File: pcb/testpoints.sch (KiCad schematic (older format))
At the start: 0 parts

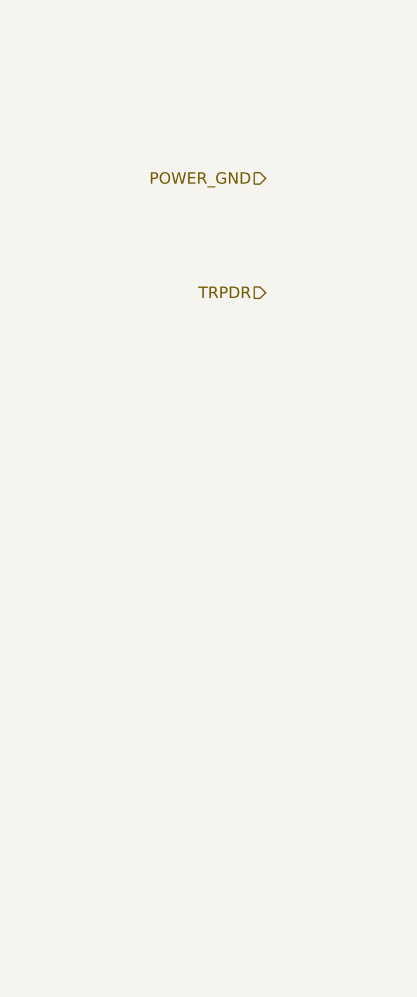
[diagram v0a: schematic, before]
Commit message: buffer section finished, audio moved to expansion connector
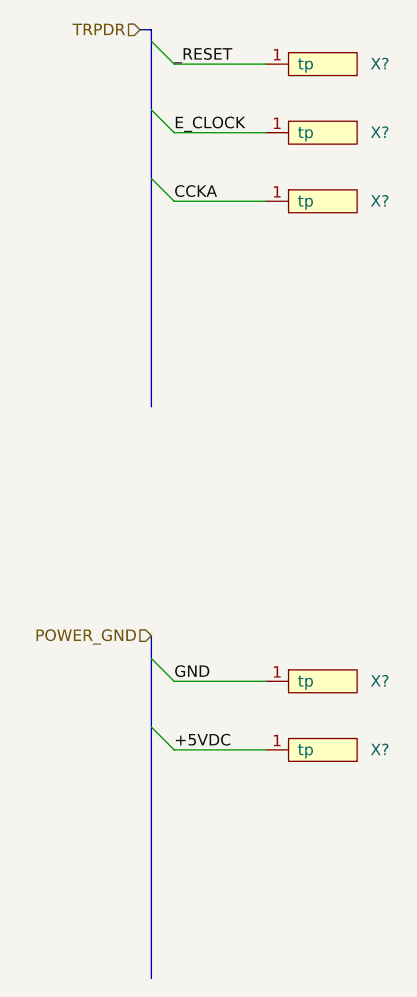
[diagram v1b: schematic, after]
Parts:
- added X? (x5): testpoint, symbol WM1200:testpoint
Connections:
- new net +5VDC: X?.1 (tp)
- new net CCKA: X?.1 (tp)
- new net E_CLOCK: X?.1 (tp)
- new net GND: X?.1 (tp)
- new net _RESET: X?.1 (tp)
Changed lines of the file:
@@
 Comment4 ""
 $EndDescr
-Text HLabel 1500 1500 0    50   Input ~ 0
+Text HLabel 1000 3500 0    50   Input ~ 0
 POWER_GND
-Text HLabel 1500 2000 0    50   Input ~ 0
+Text HLabel 950  850  0    50   Input ~ 0
 TRPDR
+$Comp
+L WM1200:testpoint X?
+U 1 1 5E702FA3
+P 1750 1050
+F 0 "X?" H 2000 1100 50  0000 C CNN
+F 1 "testpoint" H 1750 1200 50  0001 C CNN
+F 2 "" H 1750 1050 50  0001 C CNN
+F 3 "" H 1750 1050 50  0001 C CNN
+	1    1750 1050
+	1    0    0    -1
+$EndComp
+$Comp
+L WM1200:testpoint X?
+U 1 1 5E70432E
+P 1750 1350
+F 0 "X?" H 2000 1400 50  0000 C CNN
+F 1 "testpoint" H 1750 1500 50  0001 C CNN
+F 2 "" H 1750 1350 50  0001 C CNN
+F 3 "" H 1750 1350 50  0001 C CNN
+	1    1750 1350
+	1    0    0    -1
+$EndComp
+$Comp
+L WM1200:testpoint X?
+U 1 1 5E705858
+P 1750 1650
+F 0 "X?" H 2000 1700 50  0000 C CNN
+F 1 "testpoint" H 1750 1800 50  0001 C CNN
+F 2 "" H 1750 1650 50  0001 C CNN
+F 3 "" H 1750 1650 50  0001 C CNN
+	1    1750 1650
+	1    0    0    -1
+$EndComp
+Wire Bus Line
+	1000 850  950  850
+Entry Wire Line
+	1000 900  1100 1000
+Entry Wire Line
+	1000 1200 1100 1300
+Entry Wire Line
+	1000 1500 1100 1600
+Wire Wire Line
+	1100 1000 1500 1000
+Wire Wire Line
+	1500 1300 1100 1300
+Wire Wire Line
+	1100 1600 1500 1600
+Text Label 1100 1000 0    50   ~ 0
+_RESET
+Text Label 1100 1300 0    50   ~ 0
+E_CLOCK
+Text Label 1100 1600 0    50   ~ 0
+CCKA
+$Comp
+L WM1200:testpoint X?
+U 1 1 5E70BC9E
+P 1750 3750
+F 0 "X?" H 2000 3800 50  0000 C CNN
+F 1 "testpoint" H 1750 3900 50  0001 C CNN
+F 2 "" H 1750 3750 50  0001 C CNN
+F 3 "" H 1750 3750 50  0001 C CNN
+	1    1750 3750
+	1    0    0    -1
+$EndComp
+$Comp
+L WM1200:testpoint X?
+U 1 1 5E70BCA4
+P 1750 4050
+F 0 "X?" H 2000 4100 50  0000 C CNN
+F 1 "testpoint" H 1750 4200 50  0001 C CNN
+F 2 "" H 1750 4050 50  0001 C CNN
+F 3 "" H 1750 4050 50  0001 C CNN
+	1    1750 4050
+	1    0    0    -1
+$EndComp
+Entry Wire Line
+	1000 3600 1100 3700
+Entry Wire Line
+	1000 3900 1100 4000
+Wire Wire Line
+	1100 3700 1500 3700
+Wire Wire Line
+	1500 4000 1100 4000
+Text Label 1100 3700 0    50   ~ 0
+GND
+Text Label 1100 4000 0    50   ~ 0
++5VDC
+Wire Bus Line
+	1000 3500 1000 5000
+Wire Bus Line
+	1000 850  1000 2500
 $EndSCHEMATC

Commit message: Some work done on the whole project
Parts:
- gave numbers to parts that had none: 5
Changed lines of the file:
@@
 TRPDR
 $Comp
-L WM1200:testpoint X?
+L WM1200:testpoint XT1
 U 1 1 5E702FA3
 P 1750 1050
-F 0 "X?" H 2000 1100 50  0000 C CNN
+F 0 "XT1" H 2000 1100 50  0000 C CNN
 F 1 "testpoint" H 1750 1200 50  0001 C CNN
 F 2 "" H 1750 1050 50  0001 C CNN
@@
 $EndComp
 $Comp
-L WM1200:testpoint X?
+L WM1200:testpoint XT2
 U 1 1 5E70432E
 P 1750 1350
-F 0 "X?" H 2000 1400 50  0000 C CNN
+F 0 "XT2" H 2000 1400 50  0000 C CNN
 F 1 "testpoint" H 1750 1500 50  0001 C CNN
 F 2 "" H 1750 1350 50  0001 C CNN
@@
 $EndComp
 $Comp
-L WM1200:testpoint X?
+L WM1200:testpoint XT3
 U 1 1 5E705858
 P 1750 1650
-F 0 "X?" H 2000 1700 50  0000 C CNN
+F 0 "XT3" H 2000 1700 50  0000 C CNN
 F 1 "testpoint" H 1750 1800 50  0001 C CNN
 F 2 "" H 1750 1650 50  0001 C CNN
@@
 CCKA
 $Comp
-L WM1200:testpoint X?
+L WM1200:testpoint XT4
 U 1 1 5E70BC9E
 P 1750 3750
-F 0 "X?" H 2000 3800 50  0000 C CNN
+F 0 "XT4" H 2000 3800 50  0000 C CNN
 F 1 "testpoint" H 1750 3900 50  0001 C CNN
 F 2 "" H 1750 3750 50  0001 C CNN
@@
 $EndComp
 $Comp
-L WM1200:testpoint X?
+L WM1200:testpoint XT5
 U 1 1 5E70BCA4
 P 1750 4050
-F 0 "X?" H 2000 4100 50  0000 C CNN
+F 0 "XT5" H 2000 4100 50  0000 C CNN
 F 1 "testpoint" H 1750 4200 50  0001 C CNN
 F 2 "" H 1750 4050 50  0001 C CNN

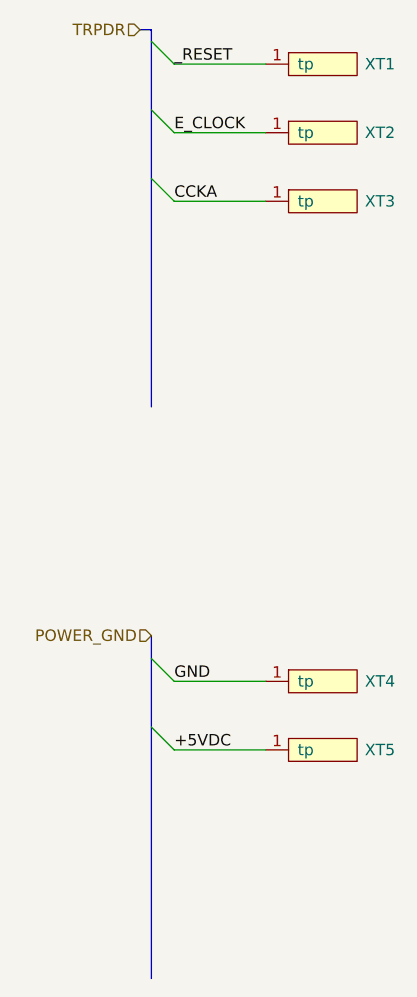
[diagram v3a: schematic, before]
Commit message: ok, we are using global labels now
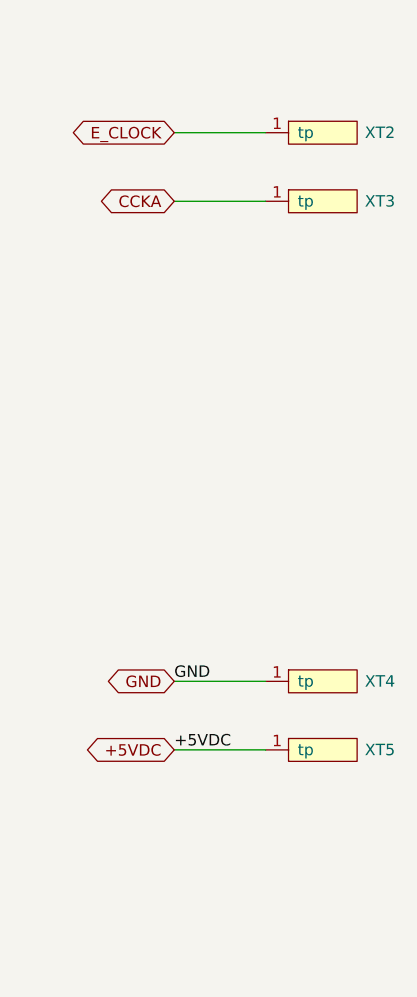
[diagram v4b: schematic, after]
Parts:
- removed XT1: testpoint, symbol WM1200:testpoint
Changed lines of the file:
@@
 $Descr A4 11693 8268
 encoding utf-8
-Sheet 4 11
+Sheet 2 11
 Title "WishMaster 1200"
 Date ""
@@
 Comment4 ""
 $EndDescr
-Text HLabel 1000 3500 0    50   Input ~ 0
-POWER_GND
-Text HLabel 950  850  0    50   Input ~ 0
-TRPDR
-$Comp
-L WM1200:testpoint XT1
-U 1 1 5E702FA3
-P 1750 1050
-F 0 "XT1" H 2000 1100 50  0000 C CNN
-F 1 "testpoint" H 1750 1200 50  0001 C CNN
-F 2 "" H 1750 1050 50  0001 C CNN
-F 3 "" H 1750 1050 50  0001 C CNN
-	1    1750 1050
-	1    0    0    -1
-$EndComp
 $Comp
 L WM1200:testpoint XT2
@@
 	1    0    0    -1
 $EndComp
-Wire Bus Line
-	1000 850  950  850
-Entry Wire Line
-	1000 900  1100 1000
-Entry Wire Line
-	1000 1200 1100 1300
-Entry Wire Line
-	1000 1500 1100 1600
-Wire Wire Line
-	1100 1000 1500 1000
 Wire Wire Line
 	1500 1300 1100 1300
 Wire Wire Line
 	1100 1600 1500 1600
-Text Label 1100 1000 0    50   ~ 0
-_RESET
-Text Label 1100 1300 0    50   ~ 0
-E_CLOCK
-Text Label 1100 1600 0    50   ~ 0
-CCKA
 $Comp
 L WM1200:testpoint XT4
@@
 	1    0    0    -1
 $EndComp
-Entry Wire Line
-	1000 3600 1100 3700
-Entry Wire Line
-	1000 3900 1100 4000
 Wire Wire Line
 	1100 3700 1500 3700
@@
 Text Label 1100 4000 0    50   ~ 0
 +5VDC
-Wire Bus Line
-	1000 3500 1000 5000
-Wire Bus Line
-	1000 850  1000 2500
+Text GLabel 1100 1300 0    50   BiDi ~ 0
+E_CLOCK
+Text GLabel 1100 1600 0    50   BiDi ~ 0
+CCKA
+Text GLabel 1100 3700 0    50   BiDi ~ 0
+GND
+Text GLabel 1100 4000 0    50   BiDi ~ 0
++5VDC
 $EndSCHEMATC

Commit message: fpga-side gpio connector added
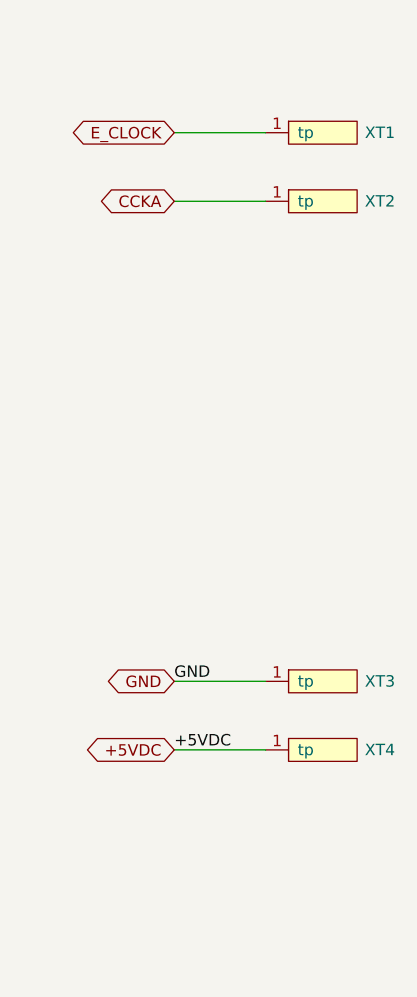
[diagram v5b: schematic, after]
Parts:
- renumbered XT2 to XT1, XT3 to XT2, XT4 to XT3, XT5 to XT4
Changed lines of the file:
@@
 $EndDescr
 $Comp
-L WM1200:testpoint XT2
+L WM1200:testpoint XT1
 U 1 1 5E70432E
 P 1750 1350
-F 0 "XT2" H 2000 1400 50  0000 C CNN
+F 0 "XT1" H 2000 1400 50  0000 C CNN
 F 1 "testpoint" H 1750 1500 50  0001 C CNN
 F 2 "" H 1750 1350 50  0001 C CNN
@@
 $EndComp
 $Comp
-L WM1200:testpoint XT3
+L WM1200:testpoint XT2
 U 1 1 5E705858
 P 1750 1650
-F 0 "XT3" H 2000 1700 50  0000 C CNN
+F 0 "XT2" H 2000 1700 50  0000 C CNN
 F 1 "testpoint" H 1750 1800 50  0001 C CNN
 F 2 "" H 1750 1650 50  0001 C CNN
@@
 	1100 1600 1500 1600
 $Comp
-L WM1200:testpoint XT4
+L WM1200:testpoint XT3
 U 1 1 5E70BC9E
 P 1750 3750
-F 0 "XT4" H 2000 3800 50  0000 C CNN
+F 0 "XT3" H 2000 3800 50  0000 C CNN
 F 1 "testpoint" H 1750 3900 50  0001 C CNN
 F 2 "" H 1750 3750 50  0001 C CNN
@@
 $EndComp
 $Comp
-L WM1200:testpoint XT5
+L WM1200:testpoint XT4
 U 1 1 5E70BCA4
 P 1750 4050
-F 0 "XT5" H 2000 4100 50  0000 C CNN
+F 0 "XT4" H 2000 4100 50  0000 C CNN
 F 1 "testpoint" H 1750 4200 50  0001 C CNN
 F 2 "" H 1750 4050 50  0001 C CNN

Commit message: more footprints assigned
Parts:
- XT1, XT2, XT3, XT4: footprint (none) -> WM1200:testpoint
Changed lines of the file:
@@
 F 0 "XT1" H 2000 1400 50  0000 C CNN
 F 1 "testpoint" H 1750 1500 50  0001 C CNN
-F 2 "" H 1750 1350 50  0001 C CNN
+F 2 "WM1200:testpoint" H 1750 1350 50  0001 C CNN
 F 3 "" H 1750 1350 50  0001 C CNN
 	1    1750 1350
@@
 F 0 "XT2" H 2000 1700 50  0000 C CNN
 F 1 "testpoint" H 1750 1800 50  0001 C CNN
-F 2 "" H 1750 1650 50  0001 C CNN
+F 2 "WM1200:testpoint" H 1750 1650 50  0001 C CNN
 F 3 "" H 1750 1650 50  0001 C CNN
 	1    1750 1650
@@
 F 0 "XT3" H 2000 3800 50  0000 C CNN
 F 1 "testpoint" H 1750 3900 50  0001 C CNN
-F 2 "" H 1750 3750 50  0001 C CNN
+F 2 "WM1200:testpoint" H 1750 3750 50  0001 C CNN
 F 3 "" H 1750 3750 50  0001 C CNN
 	1    1750 3750
@@
 F 0 "XT4" H 2000 4100 50  0000 C CNN
 F 1 "testpoint" H 1750 4200 50  0001 C CNN
-F 2 "" H 1750 4050 50  0001 C CNN
+F 2 "WM1200:testpoint" H 1750 4050 50  0001 C CNN
 F 3 "" H 1750 4050 50  0001 C CNN
 	1    1750 4050

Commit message: Board pcb updated
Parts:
- removed XT1, XT2, XT3, XT4: testpoint, WM1200:testpoint, symbol WM1200:testpoint
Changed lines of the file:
@@
 Comment4 ""
 $EndDescr
-$Comp
-L WM1200:testpoint XT1
-U 1 1 5E70432E
-P 1750 1350
-F 0 "XT1" H 2000 1400 50  0000 C CNN
-F 1 "testpoint" H 1750 1500 50  0001 C CNN
-F 2 "WM1200:testpoint" H 1750 1350 50  0001 C CNN
-F 3 "" H 1750 1350 50  0001 C CNN
-	1    1750 1350
-	1    0    0    -1
-$EndComp
-$Comp
-L WM1200:testpoint XT2
-U 1 1 5E705858
-P 1750 1650
-F 0 "XT2" H 2000 1700 50  0000 C CNN
-F 1 "testpoint" H 1750 1800 50  0001 C CNN
-F 2 "WM1200:testpoint" H 1750 1650 50  0001 C CNN
-F 3 "" H 1750 1650 50  0001 C CNN
-	1    1750 1650
-	1    0    0    -1
-$EndComp
-Wire Wire Line
-	1500 1300 1100 1300
-Wire Wire Line
-	1100 1600 1500 1600
-$Comp
-L WM1200:testpoint XT3
-U 1 1 5E70BC9E
-P 1750 3750
-F 0 "XT3" H 2000 3800 50  0000 C CNN
-F 1 "testpoint" H 1750 3900 50  0001 C CNN
-F 2 "WM1200:testpoint" H 1750 3750 50  0001 C CNN
-F 3 "" H 1750 3750 50  0001 C CNN
-	1    1750 3750
-	1    0    0    -1
-$EndComp
-$Comp
-L WM1200:testpoint XT4
-U 1 1 5E70BCA4
-P 1750 4050
-F 0 "XT4" H 2000 4100 50  0000 C CNN
-F 1 "testpoint" H 1750 4200 50  0001 C CNN
-F 2 "WM1200:testpoint" H 1750 4050 50  0001 C CNN
-F 3 "" H 1750 4050 50  0001 C CNN
-	1    1750 4050
-	1    0    0    -1
-$EndComp
-Wire Wire Line
-	1100 3700 1500 3700
-Wire Wire Line
-	1500 4000 1100 4000
-Text Label 1100 3700 0    50   ~ 0
-GND
-Text Label 1100 4000 0    50   ~ 0
-+5VDC
-Text GLabel 1100 1300 0    50   BiDi ~ 0
-E_CLOCK
-Text GLabel 1100 1600 0    50   BiDi ~ 0
-CCKA
-Text GLabel 1100 3700 0    50   BiDi ~ 0
-GND
-Text GLabel 1100 4000 0    50   BiDi ~ 0
-+5VDC
 $EndSCHEMATC
